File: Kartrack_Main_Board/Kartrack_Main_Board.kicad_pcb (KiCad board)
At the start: 2 copper layers, 130 x 80 mm, 1 part

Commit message: FIn de séance
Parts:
- removed A1: Arduino_UNO_R3, Module:Arduino_UNO_R3
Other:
- board outline removed

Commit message: PCB early
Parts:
- added A2: Arduino_UNO_R3, Module:Arduino_UNO_R3, B.Cu at (208.5, 108.6)
- added C1: 470u, Capacitor_SMD:CP_Elec_8x10, F.Cu at (66.2, 87.5)
- added C10: 1uF, Capacitor_SMD:C_0603_1608Metric, F.Cu at (54.8, 76.5)
- added C11: 100pF, Capacitor_SMD:C_0603_1608Metric, F.Cu at (45.2, 102.5)
- added C12: 10nF, Capacitor_SMD:C_0603_1608Metric, F.Cu at (41.8, 142.6)
- added C13: 10nF, Capacitor_SMD:C_0603_1608Metric, F.Cu at (41.8, 145.1)
- added C14: 100nF, Capacitor_SMD:C_0402_1005Metric, F.Cu at (52.6, 115.3)
- added C15: 100nF, Capacitor_SMD:C_0402_1005Metric, F.Cu at (52.6, 117.3)
- added C16: 10nF, Capacitor_SMD:C_0603_1608Metric, F.Cu at (41.8, 147.6)
- added C17: 470nF, Capacitor_SMD:C_0603_1608Metric, F.Cu at (156.2, 126.9)
- added C18: 470nF, Capacitor_SMD:C_0603_1608Metric, F.Cu at (162.1, 128.4)
- added C3: 100nF, Capacitor_SMD:C_0603_1608Metric, F.Cu at (45.2, 92.5)
- added C4: 10uF, Capacitor_SMD:C_0603_1608Metric, F.Cu at (45.2, 95.0)
- added C5: 15pF, Capacitor_SMD:C_0603_1608Metric, F.Cu at (45.2, 97.5)
- added C6: 15pF, Capacitor_SMD:C_0603_1608Metric, F.Cu at (45.2, 100.0)
- added C7: 10uF, Capacitor_SMD:C_0603_1608Metric, F.Cu at (54.8, 71.4)
- added C9: 15pf, Capacitor_SMD:C_0603_1608Metric, F.Cu at (54.8, 74.0)
- added D1: 1N4148WS, Diode_SMD:D_SOD-323, F.Cu at (51.4, 107.8)
- added D2: LED, LED_SMD:LED_0603_1608Metric, F.Cu at (144.3, 134.8)
- added D3: BZX84W, Package_TO_SOT_SMD:SOT-23, F.Cu at (79.1, 81.8)
- added D4: STPS0520Z, Diode_SMD:D_SOD-123, F.Cu at (20.4, 73.6)
- added IC1: MIC3172YM, MIC3172:SOIC127P599X173-8N, F.Cu at (146.0, 117.4)
- added J1: USB_C_Receptacle_USB2.0_14P, Connector_USB:USB_C_Receptacle_GCT_USB4125-xx-x-0190_6P_TopMnt_Horizontal, F.Cu at (150.8, 136.6)
- added J2: Conn_Coaxial, Connector_Coaxial:U.FL_Molex_MCRF_73412-0110_Vertical, F.Cu at (46.2, 109.4)
- added J3: Conn_Coaxial, Connector_Coaxial:U.FL_Molex_MCRF_73412-0110_Vertical, F.Cu at (27.6, 136.5)
- added J4: Conn_01x02_Socket, Battery:BatteryHolder_MPD_BH-18650-PC2, F.Cu at (112.0, 136.6)
- added J5: Conn_01x02_Socket, Battery:BatteryHolder_MPD_BH-18650-PC2, F.Cu at (133.0, 136.6)
- added L1: 47nF, Inductor_SMD:L_0603_1608Metric, F.Cu at (45.2, 105.0)
- added L2: 100uH, Inductor_SMD:L_12x12mm_H8mm, F.Cu at (45.4, 77.3)
- added MT1: ICM-45605, ICM-45605:IC_ICM-45605, F.Cu at (48.9, 116.4)
- added Q1: RE1C, Package_TO_SOT_SMD:SOT-416, F.Cu at (26.6, 110.2)
- added R1: 5.1k, Resistor_SMD:R_0603_1608Metric, F.Cu at (41.8, 150.1)
- added R10: 1k, Resistor_SMD:R_0603_1608Metric, F.Cu at (144.3, 137.9)
- added R11: 0, Resistor_SMD:R_0603_1608Metric, F.Cu at (58.8, 76.5)
- added R12: 3,74k, Resistor_SMD:R_0603_1608Metric, F.Cu at (58.8, 79.0)
- added R13: 1,24k, Resistor_SMD:R_0603_1608Metric, F.Cu at (58.8, 81.5)
- added R14: 250R, Resistor_SMD:R_0603_1608Metric, F.Cu at (149.1, 125.2)
- added R15: 0, Resistor_SMD:R_0603_1608Metric, F.Cu at (62.8, 74.0)
- added R16: 1k, Resistor_SMD:R_0603_1608Metric, F.Cu at (62.8, 76.5)
- added R17: 0, Resistor_SMD:R_0603_1608Metric, F.Cu at (53.2, 92.5)
- added R18: 0, Resistor_SMD:R_0603_1608Metric, F.Cu at (53.2, 95.0)
- added R19: 0, Resistor_SMD:R_0603_1608Metric, F.Cu at (53.2, 97.5)
- added R2: 5.1k, Resistor_SMD:R_0603_1608Metric, F.Cu at (41.8, 152.6)
- added R22: 100R, Resistor_SMD:R_0603_1608Metric, F.Cu at (54.8, 101.8)
- added R23: 10K, Resistor_SMD:R_0603_1608Metric, F.Cu at (41.8, 155.1)
- added R24: 10K, Resistor_SMD:R_0603_1608Metric, F.Cu at (45.8, 142.6)
- added R25: 10K, Resistor_SMD:R_0603_1608Metric, F.Cu at (45.8, 145.1)
- added R26: 10K, Resistor_SMD:R_0603_1608Metric, F.Cu at (45.8, 147.6)
- added R27: 10K, Resistor_SMD:R_0603_1608Metric, F.Cu at (45.8, 150.1)
- added R28: 10K, Resistor_SMD:R_0603_1608Metric, F.Cu at (45.8, 152.6)
- added R3: 10k, Resistor_SMD:R_0603_1608Metric, F.Cu at (49.2, 92.5)
- added R4: 1k, Resistor_SMD:R_0603_1608Metric, F.Cu at (49.2, 95.0)
- added R5: 1k, Resistor_SMD:R_0603_1608Metric, F.Cu at (49.2, 97.5)
- added R6: 10k, Resistor_SMD:R_0603_1608Metric, F.Cu at (49.2, 100.0)
- added R7: 4.7k, Resistor_SMD:R_0603_1608Metric, F.Cu at (49.2, 102.5)
- added R8: 4.7k, Resistor_SMD:R_0603_1608Metric, F.Cu at (49.2, 105.0)
- added R9: 10k, Resistor_SMD:R_0603_1608Metric, F.Cu at (147.3, 129.0)
- added SW1: SW_Push, Connector_PinSocket_2.54mm:PinSocket_1x02_P2.54mm_Vertical_SMD_Pin1Left, F.Cu at (21.6, 145.1)
- added SW2: SW_Push, Connector_PinSocket_2.54mm:PinSocket_1x02_P2.54mm_Vertical_SMD_Pin1Left, F.Cu at (28.9, 145.1)
- added SW3: SW_Push, Connector_PinSocket_2.54mm:PinSocket_1x02_P2.54mm_Vertical_SMD_Pin1Left, F.Cu at (36.1, 145.1)
- added U2: L76L-M33, L76L-M33:XCVR_L76L-M33, F.Cu at (33.9, 99.9)
- added U3: Ai-Thinker-Ra-02, RF_Module:Ai-Thinker-Ra-01-LoRa, F.Cu at (34.4, 123.9)
- added U4: BQ21040DBV, Package_TO_SOT_SMD:SOT-23-6, F.Cu at (146.3, 125.6)
- added U5: BU33SD5WG, Package_TO_SOT_SMD:SOT-23-5, F.Cu at (159.1, 128.6)
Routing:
- net +5V: track 0.00 -> 14.9 mm, vias 0 -> 9
- net Net-(D2-K): track 0.00 -> 8.51 mm
- net +3.3V: track 0.00 -> 3.38 mm, vias 0 -> 1
- net Net-(U4-ISET): track 0.00 -> 1.92 mm
- net Net-(D2-A): track 0.00 -> 1.49 mm
- net GND: vias 0 -> 1
- added copper zone on In2.Cu, net +3.3V
- added copper zone on F.Cu, net +5V
- added copper zone on In1.Cu, net +5V
- added copper zone on F.Cu, net +BATT
- added copper zone on B.Cu, net GND
- added copper zone on F.Cu, net GND
- added copper zone on In1.Cu, net GND
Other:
- board outline added: 199.4 x 82.3 mm
- copper layers 2 -> 4

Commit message: Routing alim
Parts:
- removed C9: 15pf, Capacitor_SMD:C_0603_1608Metric
- moved D4 141.8 mm to (153.9, 121.4)
- moved L2 107.4 mm to (150.8, 97.7)
- moved C1 106.7 mm to (166.7, 123.5)
- moved C7 104.5 mm to (148.8, 117.0)
- moved C10 103.0 mm to (153.6, 105.5), turned to 180 degrees
- moved R12 102.3 mm to (154.4, 115.5)
- moved R13 100.8 mm to (154.4, 113.3), turned to 180 degrees
- moved R16 97.2 mm to (154.4, 109.0), turned to 90 degrees
- moved R11 93.5 mm to (147.2, 107.1)
- moved R15 90.9 mm to (148.1, 105.5)
- moved D3 82.9 mm to (153.5, 118.5), turned to 180 degrees
- moved U2 36.9 mm to (70.7, 97.1)
- moved IC1 6.55 mm to (149.9, 112.2)
- moved C17 5.55 mm to (161.5, 128.7)
- moved U5 5.55 mm to (164.4, 130.3)
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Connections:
- net Net-(D4-A) renamed /ALIM/vsw
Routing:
- net Net-(IC1-FB): track 0.00 -> 10.8 mm
- net Net-(IC1-COMP): track 0.00 -> 6.43 mm
- net Net-(IC1-~{SYNC}/EN): track 0.00 -> 4.54 mm
- net Net-(C10-Pad1): track 0.00 -> 2.65 mm
- net +5V: vias 9 -> 13
- net GND: vias 1 -> 4
- added copper zone on F.Cu, net /ALIM/vsw

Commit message: pcb
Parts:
- removed R19: 0, Resistor_SMD:R_0603_1608Metric
- added JP1: SolderJumper_2_Open, Jumper:SolderJumper-2_P1.3mm_Open_RoundedPad1.0x1.5mm, F.Cu at (212.6, 90.6)
- added JP2: SolderJumper_2_Open, Jumper:SolderJumper-2_P1.3mm_Open_RoundedPad1.0x1.5mm, F.Cu at (188.5, 65.3)
- added JP6: SolderJumper_2_Open, Jumper:SolderJumper-2_P1.3mm_Open_RoundedPad1.0x1.5mm, F.Cu at (167.8, 78.7)
- added VEXTD1: Conn_01x02_Socket, Connector_Phoenix_MC:PhoenixContact_MC_1,5_2-G-3.81_1x02_P3.81mm_Horizontal, B.Cu at (222.7, 89.8)
- moved J3 179.7 mm to (196.1, 73.9)
- moved J2 153.3 mm to (192.6, 63.9)
- moved L1 149.2 mm to (190.3, 70.4), turned to -90 degrees
- moved U3 146.8 mm to (177.5, 91.1)
- moved C11 146.1 mm to (187.9, 71.2), turned to 180 degrees
- moved C6 143.1 mm to (185.5, 71.9), turned to -90 degrees
- moved Q1 140.8 mm to (163.1, 75.7)
- moved R5 140.8 mm to (186.3, 65.5), turned to -90 degrees
- moved C5 140.7 mm to (183.5, 71.9), turned to -90 degrees
- moved R4 138.7 mm to (184.7, 65.5), turned to 90 degrees
- moved R3 136.5 mm to (183.0, 65.5), turned to -90 degrees
- moved R22 133.5 mm to (184.2, 69.1)
- moved C4 128.2 mm to (172.5, 79.8)
- moved C3 128.1 mm to (172.5, 78.2)
- moved MT1 120.8 mm to (169.7, 116.2), turned to 90 degrees
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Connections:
- A2 pad 14: /CONN/PF6_STBY_GPS -> /CONN/PF6
- A2 pad 17: /CONN/PG6 -> /CONN/PG6_STBY_GPS
- C3 pad 1: Net-(C3-Pad1) -> +3.3V
- C4 pad 1: Net-(C3-Pad1) -> +3.3V
- D1 pad 2: /CONN/PF6_STBY_GPS -> /CONN/PG6_STBY_GPS
- L1 pad 1: Net-(L1-Pad1) -> /GPS/VCC_RF
- MT1 pad 4: /CONN/PA8 -> /CONN/PG7
- MT1 pad 9: /CONN/PA15 -> /CONN/PF6
- R22 pad 2: Net-(R22-Pad2) -> /GPS/VCC_RF
- U2 pad 8: Net-(U2-VCC) -> +3.3V
- U3 pad 1: GND -> Net-(J3-In)
- U3 pad 6: /CONN/PG6 -> /CONN/PI2
- U3 pad 7: /CONN/PG7 -> /CONN/PA15
- U3 pad 8: /CONN/PI2 -> /CONN/PA8
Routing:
- net /CONN/PF8_LORA_RST: track 0.00 -> 44.0 mm
- net /CONN/PB4: track 0.00 -> 31.7 mm, vias 0 -> 1
- net /CONN/PI1_SPI2_SCK: track 0.00 -> 31.7 mm
- net /CONN/PB14_SPI2_MISO: track 0.00 -> 31.6 mm
- net /CONN/PB15_SPI2_MOSI: track 0.00 -> 31.2 mm
- net Net-(J3-In): track 0.00 -> 30.2 mm
- net /CONN/PIO_SPI2_NSS: track 0.00 -> 25.4 mm, vias 0 -> 1
- net +3.3V: track 3.38 -> 18.3 mm, vias 1 -> 6
- net /CONN/PA8: track 0.00 -> 12.5 mm
- net /CONN/PA15: track 0.00 -> 11.0 mm
- net /CONN/PI3: track 0.00 -> 11.0 mm
- net /GPS/STANDBY: track 0.00 -> 10.2 mm
- net Net-(JP1-B): track 0.00 -> 9.84 mm
- net /CONN/PI2: track 0.00 -> 9.57 mm
- net /GPS/RF_IN: track 0.00 -> 9.53 mm
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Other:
- board size 199.4 x 82.3 mm -> 175.4 x 80 mm

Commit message: PCB V1
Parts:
- removed J1: USB_C_Receptacle_USB2.0_14P, Connector_USB:USB_C_Receptacle_GCT_USB4125-xx-x-0190_6P_TopMnt_Horizontal
- added J6: USB_C_Receptacle_PowerOnly_6P, Connector_USB:USB_C_Receptacle_GCT_USB4125-xx-x_6P_TopMnt_Horizontal, F.Cu at (154.9, 136.6)
- added JP3: SolderJumper_2_Open, Jumper:SolderJumper-2_P1.3mm_Open_RoundedPad1.0x1.5mm, F.Cu at (198.8, 106.0)
- SW1, SW2, SW3: footprint Connector_PinSocket_2.54mm:PinSocket_1x02_P2.54mm_Vertical_SMD_Pin1Left -> Connector_JST:JST_PH_S2B-PH-K_1x02_P2.00mm_Horizontal
- moved SW1 184.4 mm to (218.3, 71.3), turned to 90 degrees
- moved SW2 172.9 mm to (218.3, 85.5), turned to 90 degrees
- moved SW3 168.3 mm to (218.3, 78.4), turned to 90 degrees
- moved R23 161.4 mm to (211.7, 77.1)
- moved R28 158.0 mm to (211.7, 73.9)
- moved C16 155.6 mm to (211.5, 84.0)
- moved R26 155.3 mm to (211.7, 75.5)
- moved C12 155.2 mm to (211.7, 80.6)
- moved C13 154.2 mm to (211.5, 85.7)
- moved R27 153.3 mm to (211.5, 82.4)
- moved R24 152.0 mm to (211.7, 78.9)
- moved R25 149.9 mm to (211.5, 87.3)
- moved R2 92.3 mm to (156.4, 126.1), turned to 90 degrees
- moved R1 90.3 mm to (154.8, 126.1), turned to 90 degrees
- moved R16 2.13 mm to (153.6, 107.0), turned to 0 degrees
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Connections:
- A2 pad 5: +5V -> Net-(A2-+5V)
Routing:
- net /CONN/PF6: track 0.00 -> 64.7 mm, vias 0 -> 1
- net +5V: track 14.9 -> 66.8 mm
- net /CONN/PG7: track 0.00 -> 43.6 mm, vias 0 -> 2
- net Net-(R25-Pad2): track 0.00 -> 17.2 mm
- net Net-(R27-Pad2): track 0.00 -> 15.6 mm, vias 0 -> 1
- net Net-(R23-Pad2): track 0.00 -> 14.5 mm, vias 0 -> 1
- net Net-(A2-+5V): track 0.00 -> 12.6 mm
- net +3.3V: track 18.3 -> 28.4 mm, vias 6 -> 8
- net Net-(J6-CC2): track 0.00 -> 7.50 mm
- net Net-(J6-CC1): track 0.00 -> 6.78 mm
- net /CONN/PF9_BT1: track 0.00 -> 4.15 mm
- net /CONN/PF10_BT3: track 0.00 -> 4.11 mm
- net /CONN/PA0_BT2: track 0.00 -> 3.84 mm
- net GND: track 0.00 -> 3.79 mm, vias 6 -> 17
- net Net-(IC1-COMP): track 6.43 -> 4.08 mm, vias 0 -> 2
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- added copper zone on B.Cu, net +5V
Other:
- board size 175.4 x 80 mm -> 130 x 80 mm

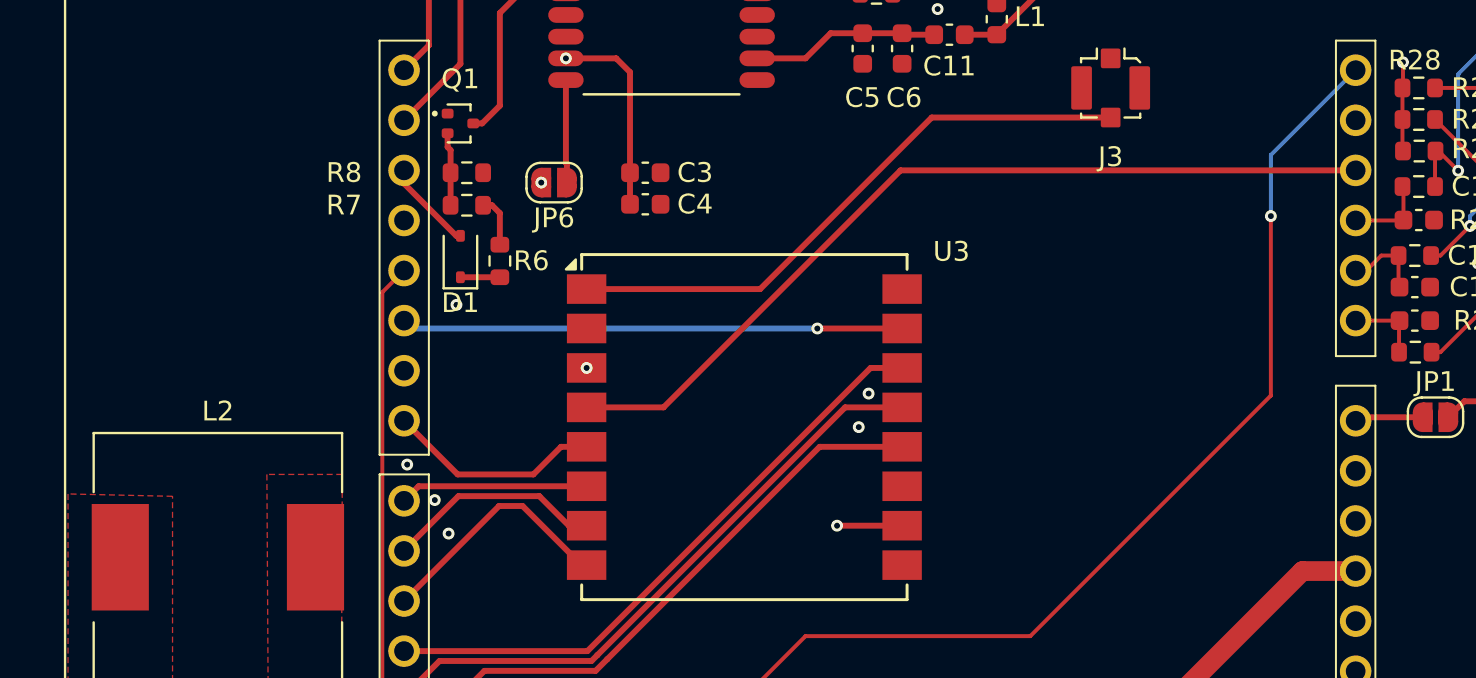
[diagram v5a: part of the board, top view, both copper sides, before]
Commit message: add adc batt
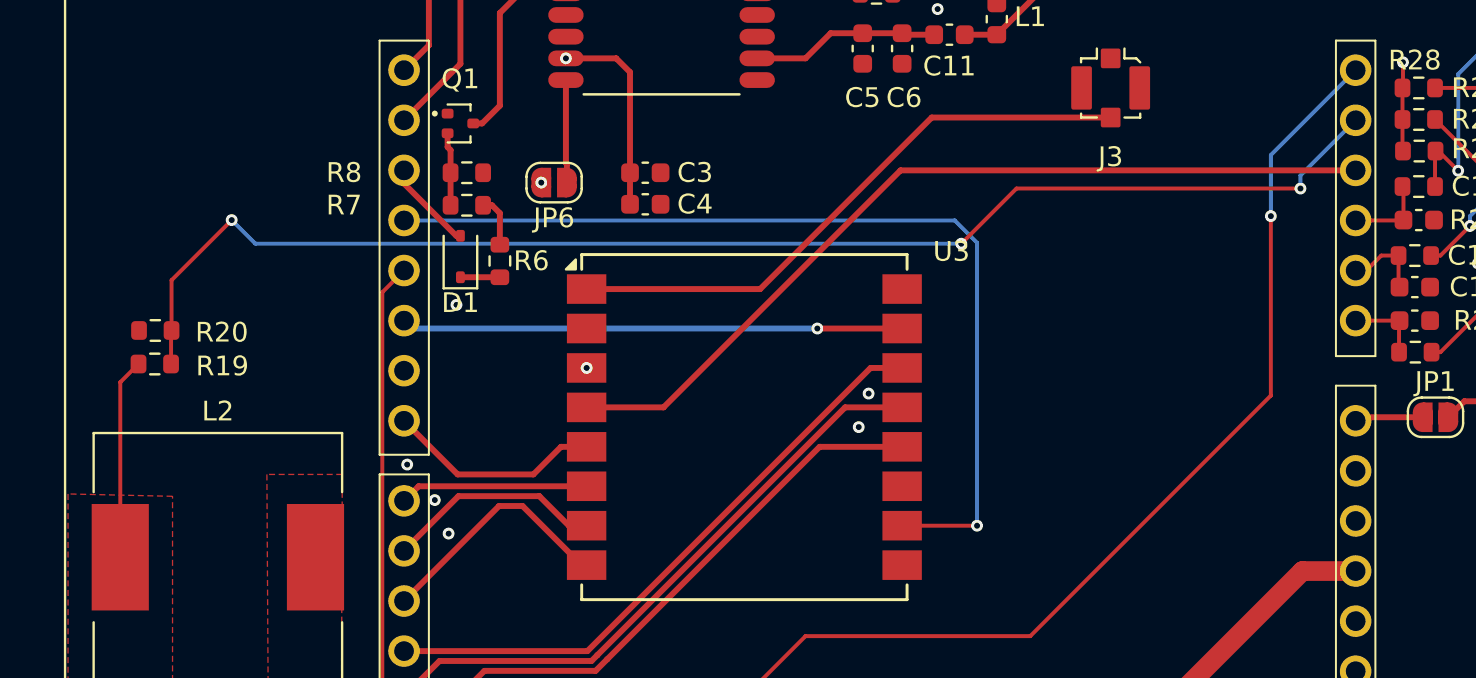
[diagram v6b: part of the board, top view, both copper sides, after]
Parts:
- added R19: 10k, Resistor_SMD:R_0603_1608Metric, F.Cu at (147.6, 87.9)
- added R20: 20k, Resistor_SMD:R_0603_1608Metric, F.Cu at (147.6, 86.2)
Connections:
- A2 pad 13: unconnected-(A2-SDA/A4-Pad13) -> /ALIM/ADC_VBATT
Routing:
- net /ALIM/ADC_VBATT: track 0.00 -> 69.1 mm, vias 0 -> 3
- net /CONN/PB4: track 31.7 -> 47.7 mm
- net +BATT: track 0.00 -> 10.2 mm

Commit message: meca update
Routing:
- net /CONN/PB4: track 47.7 -> 48.5 mm
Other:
- outline, holes or cut-outs redrawn
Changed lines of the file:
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@@
 		(layer "F.SilkS")
+	)
+	(gr_arc
+		(start 225.5 136.5)
+		(mid 224.328427 139.328427)
+		(end 221.5 140.5)
+		(stroke
+			(width 0.1)
+			(type solid)
+		)
+		(layer "Edge.Cuts")
+	)
+	(gr_line
+		(start 221.5 60.5)
+		(end 99.5 60.5)
+		(stroke
+			(width 0.05)
+			(type default)
+		)
+		(layer "Edge.Cuts")
+	)
+	(gr_arc
+		(start 95.5 64.5)
+		(mid 96.671573 61.671573)
+		(end 99.5 60.5)
+		(stroke
+			(width 0.1)
+			(type solid)
+		)
+		(layer "Edge.Cuts")
 	)
 	(gr_circle
@@
 	)
 	(gr_circle
-		(center 99 137)
-		(end 100.5 137)
+		(center 99.5 136.5)
+		(end 101 136.5)
 		(stroke
 			(width 0.1)
@@
 		(layer "Edge.Cuts")
 	)
-	(gr_circle
-		(center 185.3 120.12)
-		(end 186.8 120.12)
+	(gr_arc
+		(start 99.5 140.5)
+		(mid 96.671573 139.328427)
+		(end 95.5 136.5)
 		(stroke
 			(width 0.1)
 			(type solid)
 		)
-		(fill no)
 		(layer "Edge.Cuts")
 	)
 	(gr_circle
-		(center 221.5 136.8)
-		(end 223 136.8)
+		(center 221.5 136.5)
+		(end 223 136.5)
 		(stroke
 			(width 0.1)
@@
 		(layer "Edge.Cuts")
 	)
-	(gr_rect
-		(start 95.5 60.5)
-		(end 225.5 140.5)
-		(stroke
-			(width 0.1)
-			(type solid)
-		)
-		(fill no)
+	(gr_line
+		(start 225.5 136.5)
+		(end 225.5 64.5)
+		(stroke
+			(width 0.05)
+			(type default)
+		)
+		(layer "Edge.Cuts")
+	)
+	(gr_line
+		(start 99.5 140.5)
+		(end 221.5 140.5)
+		(stroke
+			(width 0.05)
+			(type default)
+		)
 		(layer "Edge.Cuts")
 	)
@@
 		(layer "Edge.Cuts")
 	)
+	(gr_arc
+		(start 221.5 60.5)
+		(mid 224.328427 61.671573)
+		(end 225.5 64.5)
+		(stroke
+			(width 0.1)
+			(type solid)
+		)
+		(layer "Edge.Cuts")
+	)
+	(gr_line
+		(start 95.5 64.5)
+		(end 95.5 136.5)
+		(stroke
+			(width 0.05)
+			(type default)
+		)
+		(layer "Edge.Cuts")
+	)
 	(segment
 		(start 185.5 88.1)
@@
 	)
 	(segment
-		(start 188.169943 80.62)
+		(start 189.3 96.1)
+		(end 189.3 81.2)
+		(width 0.2)
+		(layer "B.Cu")
+		(net 19)
+	)
+	(segment
+		(start 186.079518 80.8)
+		(end 185.480518 81.399)
+		(width 0.2)
+		(layer "B.Cu")
+		(net 19)
+	)
+	(segment
+		(start 185.480518 81.399)
+		(end 161.019 81.399)
+		(width 0.2)
+		(layer "B.Cu")
+		(net 19)
+	)
+	(segment
+		(start 189.3 81.2)
+		(end 188.9 80.8)
+		(width 0.2)
+		(layer "B.Cu")
+		(net 19)
+	)
+	(segment
+		(start 188.9 80.8)
+		(end 186.079518 80.8)
+		(width 0.2)
+		(layer "B.Cu")
+		(net 19)
+	)
+	(segment
+		(start 161.019 81.399)
 		(end 160.24 80.62)
-		(width 0.2)
-		(layer "B.Cu")
-		(net 19)
-	)
-	(segment
-		(start 189.3 96.1)
-		(end 189.3 81.750057)
-		(width 0.2)
-		(layer "B.Cu")
-		(net 19)
-	)
-	(segment
-		(start 189.3 81.750057)
-		(end 188.169943 80.62)
 		(width 0.2)
 		(layer "B.Cu")
@@
 	)
 	(segment
+		(start 191.769 78.531)
+		(end 205.231 78.531)
+		(width 0.2)
+		(layer "F.Cu")
+		(net 21)
+	)
+	(segment
+		(start 205.231 78.531)
+		(end 205.7 79)
+		(width 0.2)
+		(layer "F.Cu")
+		(net 21)
+	)
+	(segment
 		(start 188.5 81.8)
-		(end 191.3 79)
+		(end 191.769 78.531)
 		(width 0.2)
 		(layer "F.Cu")
@@
 		(net 21)
 	)
-	(segment
-		(start 191.3 79)
-		(end 205.7 79)
-		(width 0.2)
-		(layer "F.Cu")
-		(net 21)
-	)
 	(via
 		(at 205.7 79)
@@
 	)
 	(segment
+		(start 187.2 81.8)
+		(end 188.5 81.8)
+		(width 0.2)
+		(layer "B.Cu")
+		(net 21)
+	)
+	(segment
 		(start 205.7 79)
 		(end 205.7 78.34)
@@
 	(segment
 		(start 152.7 81.8)
-		(end 188.5 81.8)
-		(width 0.2)
-		(layer "B.Cu")
+		(end 187.2 81.8)
+		(width 0.2)
+		(layer "B.Cu")
